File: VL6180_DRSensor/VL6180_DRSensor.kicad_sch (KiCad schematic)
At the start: 20 parts, among them CN4 A1251WR-S-2P, CN5 A1251WR-S-4P, CN6 A1251WR-S-4P, Q1 BL8558-28PRN, Q2 2N7002_C916396, Q3 2N7002_C916396, Q4 2N7002_C916396, U1 1N5819W_C5451628, U2 VL6180V1NR/1

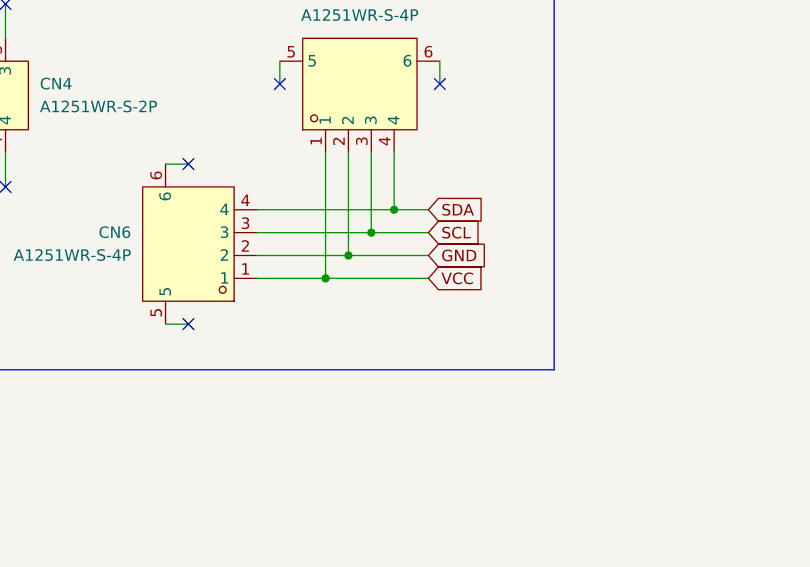
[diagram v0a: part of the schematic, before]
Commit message: Update Verison
- Screw Hole mounting version with the JST 1.25mm connectors with length tuning
- Size of the PCB is exact size as available in the market
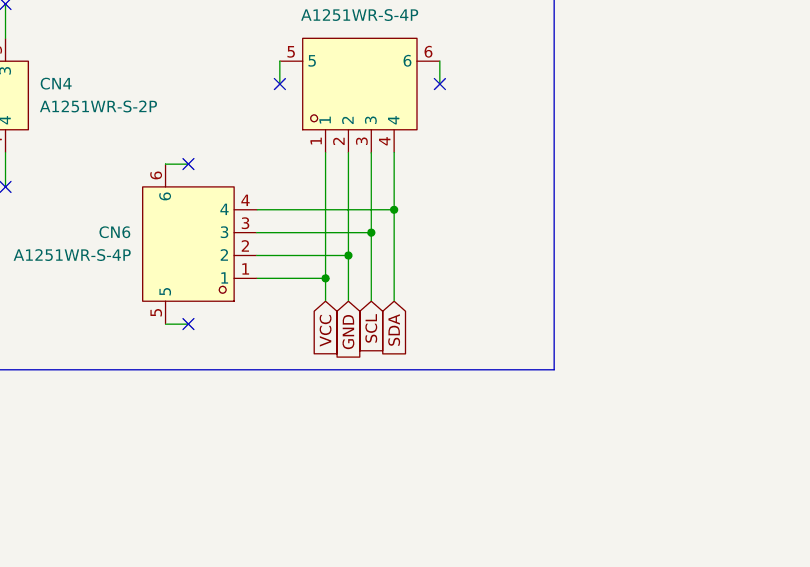
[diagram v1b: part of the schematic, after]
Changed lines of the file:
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@@
+	(wire
+		(pts
+			(xy 113.03 74.93) (xy 113.03 72.39)
+		)
+		(stroke
+			(width 0)
+			(type default)
+		)
+	)
 	(wire
 		(pts
@@
 	(wire
 		(pts
-			(xy 115.57 69.85) (xy 124.46 69.85)
-		)
-		(stroke
-			(width 0)
-			(type default)
-		)
-	)
-	(wire
-		(pts
 			(xy 76.2 118.11) (xy 76.2 127)
 		)
@@
 	(wire
 		(pts
+			(xy 115.57 74.93) (xy 115.57 69.85)
+		)
+		(stroke
+			(width 0)
+			(type default)
+		)
+	)
+	(wire
+		(pts
 			(xy 252.73 93.98) (xy 256.54 93.98)
 		)
@@
 	(wire
 		(pts
+			(xy 120.65 74.93) (xy 120.65 64.77)
+		)
+		(stroke
+			(width 0)
+			(type default)
+		)
+	)
+	(wire
+		(pts
 			(xy 80.01 129.54) (xy 82.55 129.54)
 		)
@@
 	(wire
 		(pts
+			(xy 118.11 74.93) (xy 118.11 67.31)
+		)
+		(stroke
+			(width 0)
+			(type default)
+		)
+	)
+	(wire
+		(pts
 			(xy 80.01 146.05) (xy 74.93 146.05)
 		)
@@
 	(wire
 		(pts
-			(xy 113.03 72.39) (xy 124.46 72.39)
-		)
-		(stroke
-			(width 0)
-			(type default)
-		)
-	)
-	(wire
-		(pts
-			(xy 120.65 64.77) (xy 124.46 64.77)
-		)
-		(stroke
-			(width 0)
-			(type default)
-		)
-	)
-	(wire
-		(pts
 			(xy 82.55 137.16) (xy 77.47 137.16)
 		)
@@
 	(wire
 		(pts
-			(xy 118.11 67.31) (xy 124.46 67.31)
-		)
-		(stroke
-			(width 0)
-			(type default)
-		)
-	)
-	(wire
-		(pts
 			(xy 243.84 52.07) (xy 246.38 52.07)
 		)
@@
 	(global_label "GND"
 		(shape input)
-		(at 124.46 69.85 0)
+		(at 115.57 74.93 270)
+		(fields_autoplaced yes)
+		(effects
+			(font
+				(size 1.27 1.27)
+			)
+			(justify right)
+		)
+		(property "Intersheetrefs" "${INTERSHEET_REFS}"
+			(at 115.57 81.7857 90)
+			(effects
+				(font
+					(size 1.27 1.27)
+				)
+				(justify right)
+				(hide yes)
+			)
+		)
+	)
+	(global_label "SCL_2.8V"
+		(shape input)
+		(at 257.81 107.95 0)
 		(fields_autoplaced yes)
 		(effects
@@
 		)
 		(property "Intersheetrefs" "${INTERSHEET_REFS}"
-			(at 131.3157 69.85 0)
+			(at 269.3828 107.95 0)
 			(effects
 				(font
@@
 		)
 	)
-	(global_label "SCL_2.8V"
-		(shape input)
-		(at 257.81 107.95 0)
+	(global_label "2.8V"
+		(shape input)
+		(at 255.27 46.99 0)
 		(fields_autoplaced yes)
 		(effects
@@
 		)
 		(property "Intersheetrefs" "${INTERSHEET_REFS}"
-			(at 269.3828 107.95 0)
+			(at 262.3676 46.99 0)
 			(effects
 				(font
@@
 		)
 	)
-	(global_label "2.8V"
-		(shape input)
-		(at 255.27 46.99 0)
+	(global_label "INT"
+		(shape input)
+		(at 62.23 49.53 180)
+		(fields_autoplaced yes)
+		(effects
+			(font
+				(size 1.27 1.27)
+			)
+			(justify right)
+		)
+		(property "Intersheetrefs" "${INTERSHEET_REFS}"
+			(at 56.3419 49.53 0)
+			(effects
+				(font
+					(size 1.27 1.27)
+				)
+				(justify right)
+				(hide yes)
+			)
+		)
+	)
+	(global_label "INT_2.8V"
+		(shape input)
+		(at 76.2 118.11 0)
 		(fields_autoplaced yes)
 		(effects
@@
 		)
 		(property "Intersheetrefs" "${INTERSHEET_REFS}"
-			(at 262.3676 46.99 0)
+			(at 87.1681 118.11 0)
 			(effects
 				(font
@@
 		)
 	)
-	(global_label "INT"
-		(shape input)
-		(at 62.23 49.53 180)
+	(global_label "VCC"
+		(shape input)
+		(at 113.03 74.93 270)
 		(fields_autoplaced yes)
 		(effects
@@
 		)
 		(property "Intersheetrefs" "${INTERSHEET_REFS}"
-			(at 56.3419 49.53 0)
+			(at 113.03 81.5438 90)
 			(effects
 				(font
@@
 	(global_label "INT_2.8V"
 		(shape input)
-		(at 76.2 118.11 0)
+		(at 256.54 134.62 0)
 		(fields_autoplaced yes)
 		(effects
@@
 		)
 		(property "Intersheetrefs" "${INTERSHEET_REFS}"
-			(at 87.1681 118.11 0)
+			(at 267.5081 134.62 0)
 			(effects
 				(font
@@
 		)
 	)
-	(global_label "VCC"
-		(shape input)
-		(at 124.46 72.39 0)
-		(fields_autoplaced yes)
-		(effects
-			(font
-				(size 1.27 1.27)
-			)
-			(justify left)
-		)
-		(property "Intersheetrefs" "${INTERSHEET_REFS}"
-			(at 131.0738 72.39 0)
-			(effects
-				(font
-					(size 1.27 1.27)
-				)
-				(justify left)
-				(hide yes)
-			)
-		)
-	)
-	(global_label "INT_2.8V"
-		(shape input)
-		(at 256.54 134.62 0)
-		(fields_autoplaced yes)
-		(effects
-			(font
-				(size 1.27 1.27)
-			)
-			(justify left)
-		)
-		(property "Intersheetrefs" "${INTERSHEET_REFS}"
-			(at 267.5081 134.62 0)
-			(effects
-				(font
-					(size 1.27 1.27)
-				)
-				(justify left)
-				(hide yes)
-			)
-		)
-	)
 	(global_label "SCL"
 		(shape input)
-		(at 124.46 67.31 0)
-		(fields_autoplaced yes)
-		(effects
-			(font
-				(size 1.27 1.27)
-			)
-			(justify left)
-		)
-		(property "Intersheetrefs" "${INTERSHEET_REFS}"
-			(at 130.9528 67.31 0)
-			(effects
-				(font
-					(size 1.27 1.27)
-				)
-				(justify left)
+		(at 118.11 74.93 270)
+		(fields_autoplaced yes)
+		(effects
+			(font
+				(size 1.27 1.27)
+			)
+			(justify right)
+		)
+		(property "Intersheetrefs" "${INTERSHEET_REFS}"
+			(at 118.11 81.4228 90)
+			(effects
+				(font
+					(size 1.27 1.27)
+				)
+				(justify right)
 				(hide yes)
 			)
@@
 	(global_label "SDA"
 		(shape input)
-		(at 124.46 64.77 0)
-		(fields_autoplaced yes)
-		(effects
-			(font
-				(size 1.27 1.27)
-			)
-			(justify left)
-		)
-		(property "Intersheetrefs" "${INTERSHEET_REFS}"
-			(at 131.0133 64.77 0)
-			(effects
-				(font
-					(size 1.27 1.27)
-				)
-				(justify left)
-				(hide yes)
-			)
+		(at 120.65 74.93 270)
+		(fields_autoplaced yes)
+		(effects
+			(font
+				(size 1.27 1.27)
+			)
+			(justify right)
+		)
+		(property "Intersheetrefs" "${INTERSHEET_REFS}"
+			(at 120.65 81.4833 90)
+			(effects
+				(font
+					(size 1.27 1.27)
+				)
+				(justify right)
+				(hide yes)
+			)
